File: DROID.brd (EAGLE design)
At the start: 160 x 100 mm, 82 parts

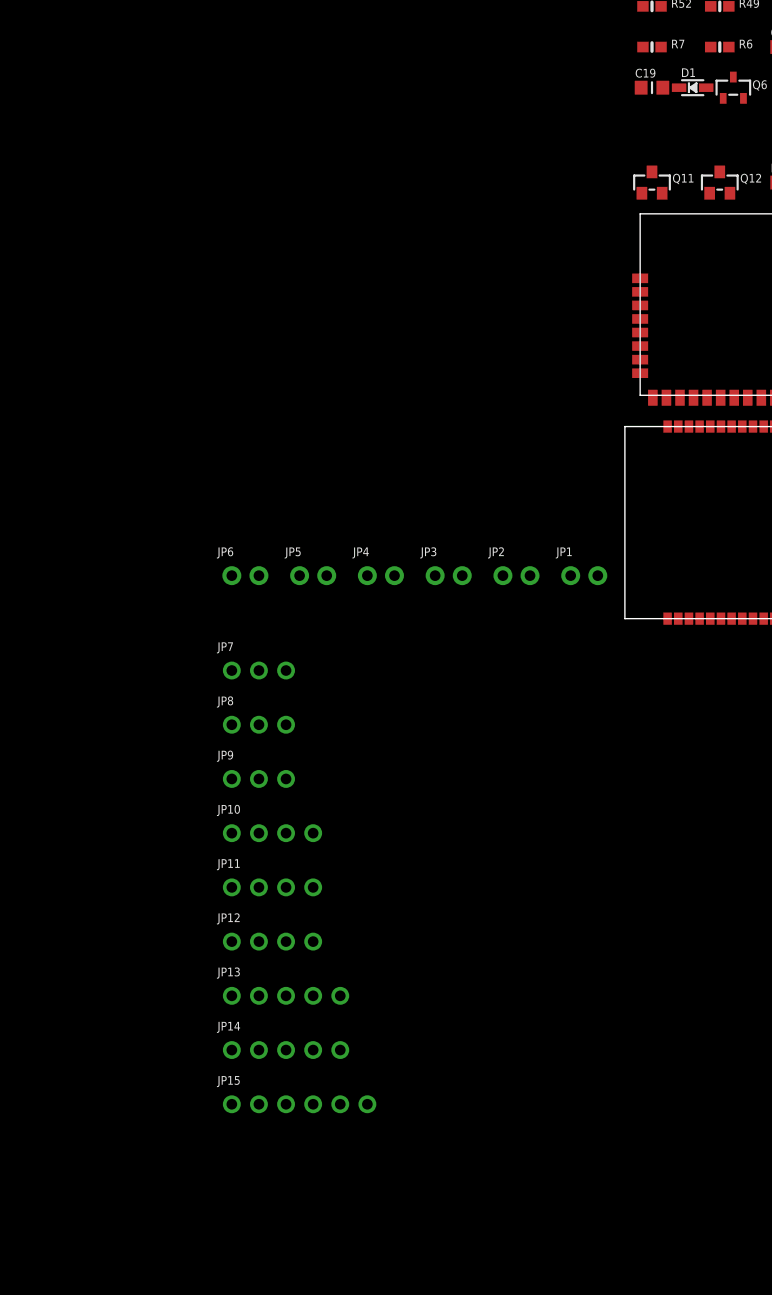
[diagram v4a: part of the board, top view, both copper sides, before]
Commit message: more nets/conns, addition parts
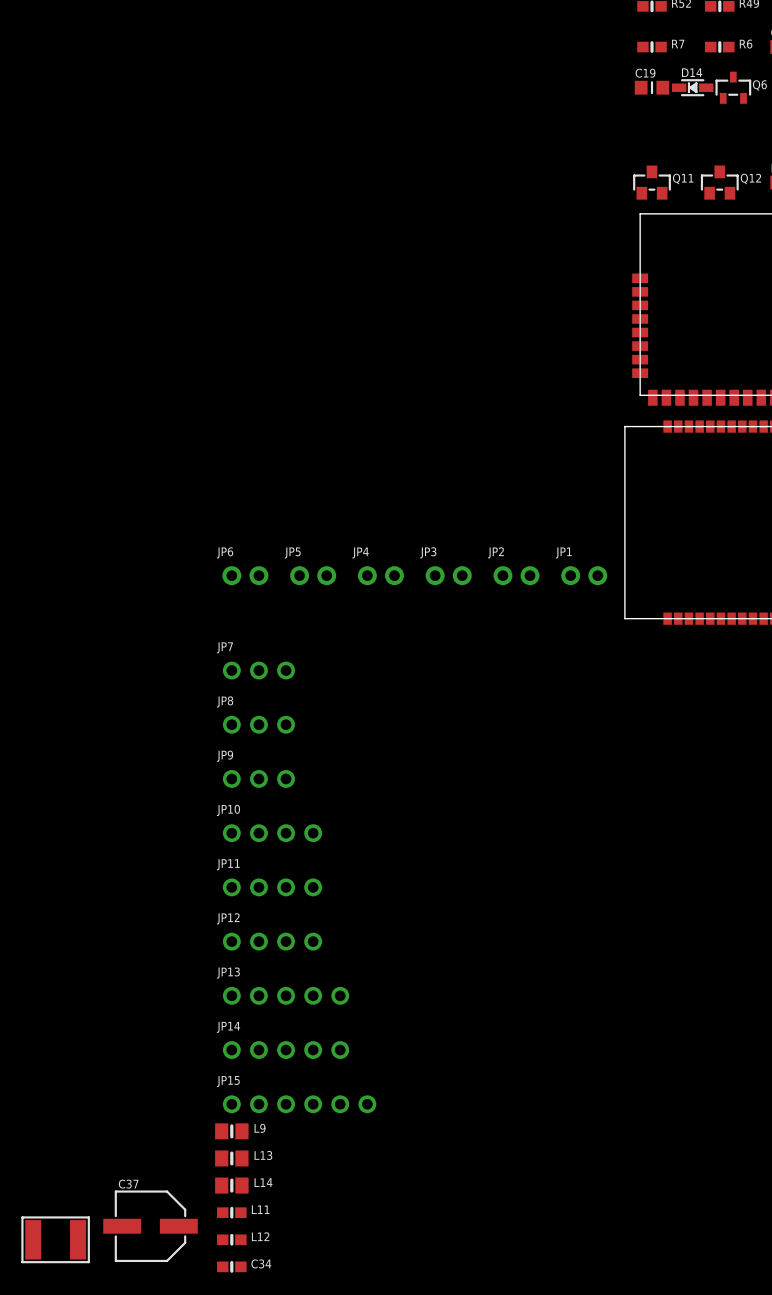
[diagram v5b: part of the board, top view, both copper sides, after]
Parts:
- added C34, L11, L12: (no value), microbuilder:0603-NO
- added C37: 100uF, microbuilder:PANASONIC_D
- added F1: (no value), microbuilder:PTC1812
- added L13, L14, L9: (no value), microbuilder:0805-NO
- renumbered D1 to D14
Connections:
- removed net C11_A: C11.1
- removed net C16_A: C16.1
- removed net C17_A: C17.1
- removed net C18_A: C18.1
- removed net C19_A: C19.1
- removed net C21_A: C21.1
- removed net C26_A: C26.1
- removed net C26_B: C26.2
- removed net C27_A: C27.1
- removed net C28_A: C28.1
- removed net C31_A: C31.1
- removed net C31_B: C31.2
- removed net C33_A: C33.1
- removed net C35_A: C35.1
- removed net C36_A: C36.1
- removed net C38_A: C38.1
- removed net HE_M_A: JP5.1
- removed net HE_M_B: JP5.2
- removed net LM_A: JP3.1
- removed net LM_B: JP3.2
- removed net N$136: U$3.6
- removed net N$144: U$2.6
- removed net N$15: R47_OR_42.1
- removed net N$152: U$1.6
- removed net N$93: C20A.1
- removed net Q11_E: Q11.2
- removed net Q12_E: Q12.2
- removed net R18_A: R18.1
- removed net R18_B: R18.2
- removed net R23_A: R23.1
- removed net R43_A: R43.1
- removed net R44_A: R44.1
- removed net R45_A: R45.1
- removed net R55_A: R55.1
- removed net R59_A: R59.1
- removed net R5_A: R5.1
- removed net R5_B: R5.2
- removed net R60_A: R60.1
- removed net R60_B: R60.2
- removed net R61_B: R61.2
- removed net R62_A: R62.1
- removed net R63_A: R63.1
- removed net R66_A: R66.1
- removed net R66_B: R66.2
- removed net R71_A: R71.1
- removed net R81_A: R81.1
- removed net R81_B: R81.2
- removed net RM_A: JP4.1
- removed net RM_B: JP4.2
- new net C34_B: C34.2
- new net D14_A: D14.A
- new net F1_1: F1.P$1
- new net F1_2: F1.P$2
- new net L11_1: L11.1
- new net L11_2: L11.2
- new net L12_1: L12.1
- new net L12_2: L12.2
- new net L13_1: L13.1
- new net L13_2: L13.2
- new net L14_1: L14.1
- new net L14_2: L14.2
- new net L9_1: L9.1
- new net L9_2: L9.2
- net GND: now also C11.1, C16.1, C17.1, C18.1, C19.1, C20A.1, C21.1, C26.2, C27.1, C28.1, C31.1, C33.1, C34.1, C35.1, C36.1, C37.-, C38.1, Q11.2, Q12.2, R43.1, R44.1, R45.1, R47_OR_42.1, R5.1, R61.2, R62.1, R63.1, R66.1, R71.1, R81.1, U$1.6, U$2.6, U$3.6
- net HEAD_OUT_B: now also JP5.1, JP5.2
- net LEFT_OUT_A: now also JP3.1
- net LEFT_OUT_B: now also JP3.2
- net OFF: now also R81.2
- net PAIR_LED-: now also R5.2
- net Q10_B: now also R60.2
- net Q11_C: now also R60.1
- net R22_A: now also R18.1
- net R23_B: now also R18.2
- net R29_A: now also R23.1
- net R61_A: now also C26.1, R55.1, R59.1
- net R64_B: now also R66.2
- net R76_B: now also C31.2
- net RIGHT_OUT_A: now also JP4.1
- net RIGHT_OUT_B: now also JP4.2
- net VCC_ON: now also C37.+, D14.C

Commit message: all components?
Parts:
- added U7, U8: (no value), microbuilder:SOT89
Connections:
- removed net C11_B: C11.2
- removed net C33_B: C33.2
- removed net C34_B: C34.2
- removed net C35_B: C35.2
- removed net C36_B: C36.2
- removed net L9_1: L9.1
- removed net L9_2: L9.2
- removed net Q10_E: Q10.2
- removed net R100_A: R100.1
- removed net R25_A: R25.1
- removed net R59_B: R59.2
- removed net R64_A: R64.1
- removed net R76_B: C31.2, R76.2
- removed net R77_B: R77.2
- removed net R99_A: R99.1
- new net U7_VIN: C34.2, U7.1
- new net U7_VOUT: C33.2, L9.2, Q10.2, U7.2, U7.2@1
- new net U8_VIN: C35.2, L9.1, U8.1
- new net U8_VOUT: C36.2, R25.1, R77.2, U8.2, U8.2@1
- net GND: now also U7.3, U8.3
- net Q10_C: now also R59.2
- net Q11_B: now also R64.1
- net Q13_B: now also R99.1
- net Q14_B: now also R100.1
- net R76_A: now also C11.2
- net VCC_33: now also C31.2, R76.2
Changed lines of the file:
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@@
 <attribute name="NAME" x="-102.235" y="-99.314" size="0.4064" layer="27" ratio="10"/>
+</element>
+<element name="U7" library="microbuilder" package="SOT89" package3d_urn="urn:adsk.eagle:package:30985/1" value="" x="-107.95" y="-93.98" smashed="yes">
+<attribute name="MF" value="" x="-107.95" y="-93.98" size="1.778" layer="27" display="off"/>
+<attribute name="MPN" value="2DB1713-13" x="-107.95" y="-93.98" size="1.778" layer="27" display="off"/>
+<attribute name="NAME" x="-110.49" y="-90.805" size="1.27" layer="25"/>
+<attribute name="OC_FARNELL" value="1710687" x="-107.95" y="-93.98" size="1.778" layer="27" display="off"/>
+<attribute name="OC_NEWARK" value="25R5670" x="-107.95" y="-93.98" size="1.778" layer="27" display="off"/>
+<attribute name="POPULARITY" value="0" x="-107.95" y="-93.98" size="1.778" layer="27" display="off"/>
+<attribute name="VALUE" x="-110.3551" y="-98.3249" size="1.27" layer="27"/>
+</element>
+<element name="U8" library="microbuilder" package="SOT89" package3d_urn="urn:adsk.eagle:package:30985/1" value="" x="-115.57" y="-93.98" smashed="yes">
+<attribute name="MF" value="" x="-115.57" y="-93.98" size="1.778" layer="27" display="off"/>
+<attribute name="MPN" value="2DB1713-13" x="-115.57" y="-93.98" size="1.778" layer="27" display="off"/>
+<attribute name="NAME" x="-118.11" y="-90.805" size="1.27" layer="25"/>
+<attribute name="OC_FARNELL" value="1710687" x="-115.57" y="-93.98" size="1.778" layer="27" display="off"/>
+<attribute name="OC_NEWARK" value="25R5670" x="-115.57" y="-93.98" size="1.778" layer="27" display="off"/>
+<attribute name="POPULARITY" value="0" x="-115.57" y="-93.98" size="1.778" layer="27" display="off"/>
+<attribute name="VALUE" x="-117.9751" y="-98.3249" size="1.27" layer="27"/>
 </element>
 </elements>
@@
 <signal name="Q14_B">
 <contactref element="Q14" pad="1"/>
+<contactref element="R100" pad="1"/>
+<wire x1="-31.33" y1="19.05" x2="-30.16" y2="10.43" width="0" layer="19" extent="1-1"/>
 </signal>
 <signal name="Q14_C">
@@
 <wire x1="-35.98" y1="19.05" x2="-38.02" y2="-17.62" width="0" layer="19" extent="1-1"/>
 </signal>
-<signal name="R100_A">
-<contactref element="R100" pad="1"/>
-</signal>
 <signal name="R100_B">
 <contactref element="R100" pad="2"/>
@@
 <wire x1="-29.63" y1="19.05" x2="-39.72" y2="-20.32" width="0" layer="19" extent="1-1"/>
 </signal>
-<signal name="R99_A">
-<contactref element="R99" pad="1"/>
-</signal>
 <signal name="R99_B">
 <contactref element="R99" pad="2"/>
@@
 <signal name="Q13_B">
 <contactref element="Q13" pad="1"/>
+<contactref element="R99" pad="1"/>
+<wire x1="-24.98" y1="19.05" x2="-23.81" y2="10.43" width="0" layer="19" extent="1-1"/>
 </signal>
 <signal name="Q13_C">
@@
 <signal name="Q10_C">
 <contactref element="Q10" pad="3"/>
-</signal>
-<signal name="Q10_E">
-<contactref element="Q10" pad="2"/>
+<contactref element="R59" pad="2"/>
+<wire x1="-23.28" y1="24.13" x2="-16.51" y2="12.43" width="0" layer="19" extent="1-1"/>
 </signal>
 <signal name="C39_A">
@@
 <contactref element="C24" pad="2"/>
 </signal>
-<signal name="C11_B">
-<contactref element="C11" pad="2"/>
-</signal>
 <signal name="C25_A">
 <contactref element="C25" pad="1"/>
@@
 <contactref element="C25" pad="2"/>
 </signal>
-<signal name="C33_B">
-<contactref element="C33" pad="2"/>
-</signal>
-<signal name="R64_A">
-<contactref element="R64" pad="1"/>
-</signal>
-<signal name="C36_B">
+<signal name="U8_VOUT">
+<contactref element="R25" pad="1"/>
+<contactref element="R77" pad="2"/>
 <contactref element="C36" pad="2"/>
+<contactref element="U8" pad="2@1" route="any" routetag="A.VOUT"/>
+<contactref element="U8" pad="2" route="any" routetag="A.VOUT"/>
+<wire x1="-24.98" y1="21.59" x2="-115.57" y2="-93.04" width="0" layer="19" extent="1-1"/>
+<wire x1="-25.82" y1="31.75" x2="-24.98" y2="21.59" width="0" layer="19" extent="1-1"/>
+<wire x1="-43.6" y1="39.37" x2="-25.82" y2="31.75" width="0" layer="19" extent="1-1"/>
 </signal>
 <signal name="R23_B">
@@
 <contactref element="C20A" pad="2"/>
 </signal>
-<signal name="R59_B">
-<contactref element="R59" pad="2"/>
-</signal>
-<signal name="R76_A">
-<contactref element="R76" pad="1"/>
-</signal>
-<signal name="R76_B">
-<contactref element="R76" pad="2"/>
-<contactref element="C31" pad="2"/>
-<wire x1="-16.93" y1="24.13" x2="-16.93" y2="39.37" width="0" layer="19" extent="1-1"/>
-</signal>
 <signal name="R68_A">
 <contactref element="R68" pad="1"/>
@@
 <signal name="R71_B">
 <contactref element="R71" pad="2"/>
-</signal>
-<signal name="R25_A">
-<contactref element="R25" pad="1"/>
 </signal>
 <signal name="R25_B">
@@
 <contactref element="R77" pad="1"/>
 </signal>
-<signal name="R77_B">
-<contactref element="R77" pad="2"/>
-</signal>
 <signal name="N$113">
 <contactref element="C22A" pad="1"/>
@@
 <contactref element="R60" pad="1"/>
 <wire x1="-44.03" y1="24.13" x2="-43.18" y2="3.54" width="0" layer="19" extent="1-1"/>
-</signal>
-<signal name="C35_B">
-<contactref element="C35" pad="2"/>
 </signal>
 <signal name="Q12_B">
@@
 <contactref element="U$4" pad="P$9"/>
 <contactref element="R5" pad="1"/>
+<contactref element="U$1" pad="6"/>
+<contactref element="U$2" pad="6"/>
+<contactref element="U$3" pad="6"/>
+<contactref element="C38" pad="1"/>
+<contactref element="C20A" pad="1"/>
+<contactref element="C21" pad="1"/>
+<contactref element="R71" pad="1"/>
+<contactref element="Q12" pad="2"/>
+<contactref element="R61" pad="2"/>
+<contactref element="C26" pad="2"/>
+<contactref element="R66" pad="1"/>
+<contactref element="C31" pad="1"/>
+<contactref element="Q11" pad="2"/>
+<contactref element="C11" pad="1"/>
+<contactref element="C37" pad="-"/>
+<contactref element="R81" pad="1"/>
+<contactref element="U7" pad="3"/>
+<contactref element="U8" pad="3"/>
 <contactref element="C36" pad="1"/>
 <contactref element="C35" pad="1"/>
@@
 <contactref element="C19" pad="1"/>
 <contactref element="C34" pad="1"/>
-<contactref element="U$1" pad="6"/>
-<contactref element="U$2" pad="6"/>
-<contactref element="U$3" pad="6"/>
-<contactref element="C38" pad="1"/>
-<contactref element="C20A" pad="1"/>
-<contactref element="C21" pad="1"/>
-<contactref element="R71" pad="1"/>
-<contactref element="Q12" pad="2"/>
-<contactref element="R61" pad="2"/>
-<contactref element="C26" pad="2"/>
-<contactref element="R66" pad="1"/>
-<contactref element="C31" pad="1"/>
-<contactref element="Q11" pad="2"/>
-<contactref element="C11" pad="1"/>
-<contactref element="C37" pad="-"/>
-<contactref element="R81" pad="1"/>
+<wire x1="-106.451" y1="-95.961" x2="-114.071" y2="-95.961" width="0" layer="19" extent="1-1"/>
+<wire x1="-92.824" y1="-95.25" x2="-106.451" y2="-95.961" width="0" layer="19" extent="1-1"/>
 <wire x1="-83.4" y1="-99.06" x2="-92.824" y2="-95.25" width="0" layer="19" extent="1-1"/>
 <wire x1="-69.85" y1="-83.82" x2="-83.4" y2="-99.06" width="0" layer="19" extent="1-1"/>
@@
 <contactref element="JP15" pad="1"/>
 <contactref element="U$4" pad="P$8"/>
+<contactref element="R76" pad="2"/>
+<contactref element="C31" pad="2"/>
 <wire x1="-74.93" y1="-68.58" x2="-82.55" y2="-83.82" width="0" layer="19" extent="1-1"/>
 <wire x1="-44.29" y1="-15.32" x2="-74.93" y2="-68.58" width="0" layer="19" extent="1-1"/>
+<wire x1="-16.93" y1="24.13" x2="-44.29" y2="-15.32" width="0" layer="19" extent="1-1"/>
+<wire x1="-16.93" y1="39.37" x2="-16.93" y2="24.13" width="0" layer="19" extent="1-1"/>
 </signal>
 <signal name="PAIR_BTN">
@@
 <contactref element="L12" pad="2"/>
 </signal>
-<signal name="L9_1">
-<contactref element="L9" pad="1"/>
-</signal>
-<signal name="L9_2">
-<contactref element="L9" pad="2"/>
-</signal>
-<signal name="C34_B">
-<contactref element="C34" pad="2"/>
-</signal>
-<signal name="Q11_B">
-<contactref element="Q11" pad="1"/>
-</signal>
 <signal name="D14_A">
 <contactref element="D14" pad="A"/>
@@
 <contactref element="JP9" pad="1"/>
 <wire x1="-29.464" y1="2.54" x2="-82.55" y2="-53.34" width="0" layer="19" extent="1-1"/>
+</signal>
+<signal name="U7_VIN">
+<contactref element="C34" pad="2"/>
+<contactref element="U7" pad="1"/>
+<wire x1="-81.7" y1="-99.06" x2="-109.449" y2="-95.961" width="0" layer="19" extent="1-1"/>
+</signal>
+<signal name="U7_VOUT">
+<contactref element="C33" pad="2"/>
+<contactref element="U7" pad="2@1" route="any" routetag="A.VOUT"/>
+<contactref element="U7" pad="2" route="any" routetag="A.VOUT"/>
+<contactref element="L9" pad="2"/>
+<contactref element="Q10" pad="2"/>
+<wire x1="-81.6" y1="-86.36" x2="-107.95" y2="-93.04" width="0" layer="19" extent="1-1"/>
+<wire x1="-15.56" y1="10.43" x2="-81.6" y2="-86.36" width="0" layer="19" extent="1-1"/>
+<wire x1="-16.93" y1="34.29" x2="-15.56" y2="10.43" width="0" layer="19" extent="1-1"/>
+</signal>
+<signal name="U8_VIN">
+<contactref element="C35" pad="2"/>
+<contactref element="U8" pad="1"/>
+<contactref element="L9" pad="1"/>
+<wire x1="-83.5" y1="-86.36" x2="-117.069" y2="-95.961" width="0" layer="19" extent="1-1"/>
+<wire x1="-42.33" y1="31.75" x2="-83.5" y2="-86.36" width="0" layer="19" extent="1-1"/>
+</signal>
+<signal name="Q11_B">
+<contactref element="R64" pad="1"/>
+<contactref element="Q11" pad="1"/>
+<wire x1="-18.63" y1="29.21" x2="-44.13" y2="1.54" width="0" layer="19" extent="1-1"/>
+</signal>
+<signal name="R76_A">
+<contactref element="C11" pad="2"/>
+<contactref element="R76" pad="1"/>
+<wire x1="-18.63" y1="24.13" x2="-29.63" y2="36.83" width="0" layer="19" extent="1-1"/>
 </signal>
 </signals>
@@
 </board>
 </drawing>
+<compatibility>
+<note version="8.3" severity="warning">
+Since Version 8.3, EAGLE supports URNs for individual library
+assets (packages, symbols, and devices). The URNs of those assets
+will not be understood (or retained) with this version.
+</note>
+<note version="8.3" severity="warning">
+Since Version 8.3, EAGLE supports the association of 3D packages
+with devices in libraries, schematics, and board files. Those 3D
+packages will not be understood (or retained) with this version.
+</note>
+</compatibility>
 </eagle>
